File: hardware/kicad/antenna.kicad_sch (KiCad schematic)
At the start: 13 parts, among them J6 BWIPX-1-001E

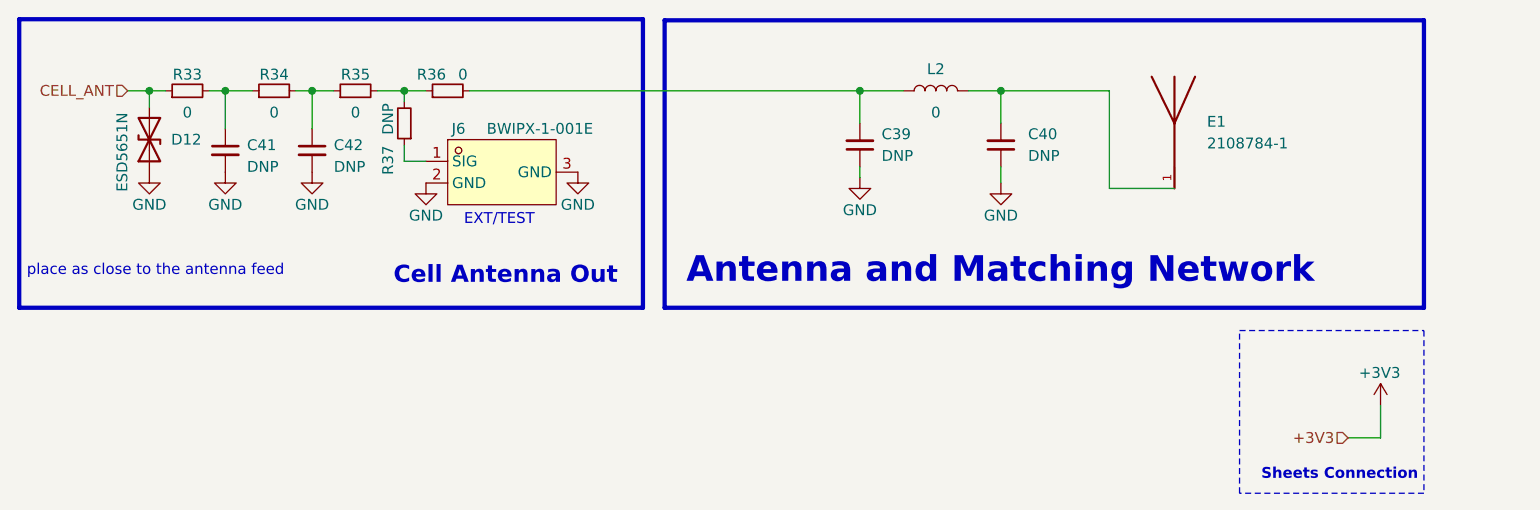
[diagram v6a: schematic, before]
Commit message: change antenna design
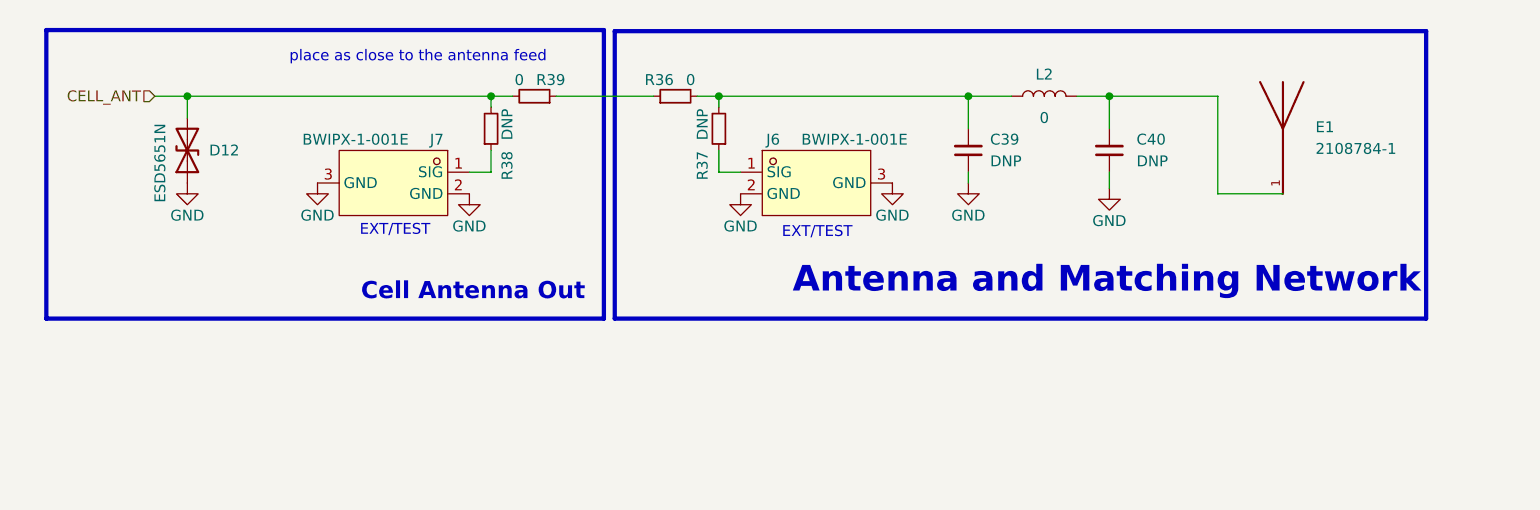
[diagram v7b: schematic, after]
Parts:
- removed C41, C42: DNP, Capacitor_SMD:C_0402_1005Metric, symbol Device:C_Small
- removed R33, R34, R35: 0, Resistor_SMD:R_0402_1005Metric, symbol Device:R_Small
- added J7: BWIPX-1-001E, bwlc1a:BWIPX-1-001E, symbol bwlc1a:BWIPX-1-001E
- added R38: DNP, Resistor_SMD:R_0402_1005Metric, symbol Device:R_Small
- added R39: 0, Resistor_SMD:R_0402_1005Metric, symbol Device:R_Small
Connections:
- net CELL_ANT: now also R38.2, R39.2
- net GND: now also J7.2 (GND), J7.3 (GND)
- net at R36.1: now also R39.1; no longer R37.2
- net at C39.2, L2.1, R36.2: now also R37.2
- new net: J7.1 (SIG), R38.1
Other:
- note removed: "Sheets Connection"
- moved on the sheet: C39, C40, D12, E1, J6, L2, R36, R37

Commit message: update
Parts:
- removed R37: DNP, Resistor_SMD:R_0402_1005Metric, symbol Device:R_Small
- added R33: DNP, Resistor_SMD:R_0402_1005Metric, symbol Device:R_Small
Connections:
- net at C39.2, L2.1, R36.2: now also R33.2
- net at J6.1 (SIG): now also R33.1
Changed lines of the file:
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@@
-	)
-	(symbol
-		(lib_id "Device:R_Small")
-		(at 153.67 93.98 180)
-		(unit 1)
-		(exclude_from_sim no)
-		(in_bom yes)
-		(on_board yes)
-		(dnp no)
-		(property "Reference" "R37"
-			(at 151.765 98.298 90)
-			(effects
-				(font
-					(size 1.27 1.27)
-				)
-			)
-		)
-		(property "Value" "DNP"
-			(at 151.765 93.472 90)
-			(effects
-				(font
-					(size 1.27 1.27)
-				)
-			)
-		)
-		(property "Footprint" "Resistor_SMD:R_0402_1005Metric"
-			(at 153.67 93.98 0)
-			(effects
-				(font
-					(size 1.27 1.27)
-				)
-				(hide yes)
-			)
-		)
-		(property "Datasheet" ""
-			(at 153.67 93.98 0)
-			(effects
-				(font
-					(size 1.27 1.27)
-				)
-				(hide yes)
-			)
-		)
-		(property "Description" ""
-			(at 153.67 93.98 0)
-			(effects
-				(font
-					(size 1.27 1.27)
-				)
-				(hide yes)
-			)
-		)
-		(property "Manufacturer" ""
-			(at 153.67 93.98 0)
-			(effects
-				(font
-					(size 1.27 1.27)
-				)
-				(hide yes)
-			)
-		)
-		(property "Manufacturer Part Number" ""
-			(at 153.67 93.98 0)
-			(effects
-				(font
-					(size 1.27 1.27)
-				)
-				(hide yes)
-			)
-		)
-		(property "Distributor" ""
-			(at 153.67 93.98 0)
-			(effects
-				(font
-					(size 1.27 1.27)
-				)
-				(hide yes)
-			)
-		)
-		(property "Distributor Part Number" ""
-			(at 153.67 93.98 0)
-			(effects
-				(font
-					(size 1.27 1.27)
-				)
-				(hide yes)
-			)
-		)
-		(property "Distributor Link" ""
-			(at 153.67 93.98 0)
-			(effects
-				(font
-					(size 1.27 1.27)
-				)
-				(hide yes)
-			)
-		)
-		(property "Id" ""
-			(at 153.67 93.98 0)
-			(effects
-				(font
-					(size 1.27 1.27)
-				)
-				(hide yes)
-			)
-		)
-		(property "Manufacture" ""
-			(at 153.67 93.98 0)
-			(effects
-				(font
-					(size 1.27 1.27)
-				)
-				(hide yes)
-			)
-		)
-		(property "Manufacture Part Number" ""
-			(at 153.67 93.98 0)
-			(effects
-				(font
-					(size 1.27 1.27)
-				)
-				(hide yes)
-			)
-		)
-		(property "Type" ""
-			(at 153.67 93.98 0)
-			(effects
-				(font
-					(size 1.27 1.27)
-				)
-				(hide yes)
-			)
-		)
-		(pin "1"
-		)
-		(pin "2"
-		)
-		(instances
-			(project "bwlc1a"
-				(path "/388039b1-99cc-430f-bd4a-010573fde798/ca79f09e-abdb-462a-9aab-98f2e37e5b23"
-					(reference "R37")
-					(unit 1)
-				)
-			)
-		)
 	)
 	(symbol
@@
 					(unit 1)
 				)
+			)
+		)
+	)
+	(symbol
+		(lib_id "Device:R_Small")
+		(at 153.67 93.98 0)
+		(mirror x)
+		(unit 1)
+		(exclude_from_sim no)
+		(in_bom yes)
+		(on_board yes)
+		(dnp no)
+		(property "Reference" "R33"
+			(at 150.876 98.298 90)
+			(effects
+				(font
+					(size 1.27 1.27)
+				)
+			)
+		)
+		(property "Value" "DNP"
+			(at 150.876 93.98 90)
+			(effects
+				(font
+					(size 1.27 1.27)
+				)
+			)
+		)
+		(property "Footprint" "Resistor_SMD:R_0402_1005Metric"
+			(at 153.67 93.98 0)
+			(effects
+				(font
+					(size 1.27 1.27)
+				)
+				(hide yes)
+			)
+		)
+		(property "Datasheet" ""
+			(at 153.67 93.98 0)
+			(effects
+				(font
+					(size 1.27 1.27)
+				)
+				(hide yes)
+			)
+		)
+		(property "Description" ""
+			(at 153.67 93.98 0)
+			(effects
+				(font
+					(size 1.27 1.27)
+				)
+				(hide yes)
+			)
+		)
+		(property "Manufacturer" ""
+			(at 153.67 93.98 0)
+			(effects
+				(font
+					(size 1.27 1.27)
+				)
+				(hide yes)
+			)
+		)
+		(property "Manufacturer Part Number" ""
+			(at 153.67 93.98 0)
+			(effects
+				(font
+					(size 1.27 1.27)
+				)
+				(hide yes)
+			)
+		)
+		(property "Distributor" ""
+			(at 153.67 93.98 0)
+			(effects
+				(font
+					(size 1.27 1.27)
+				)
+				(hide yes)
+			)
+		)
+		(property "Distributor Part Number" ""
+			(at 153.67 93.98 0)
+			(effects
+				(font
+					(size 1.27 1.27)
+				)
+				(hide yes)
+			)
+		)
+		(property "Distributor Link" ""
+			(at 153.67 93.98 0)
+			(effects
+				(font
+					(size 1.27 1.27)
+				)
+				(hide yes)
+			)
+		)
+		(property "Id" ""
+			(at 153.67 93.98 0)
+			(effects
+				(font
+					(size 1.27 1.27)
+				)
+				(hide yes)
+			)
+		)
+		(property "Manufacture" ""
+			(at 153.67 93.98 0)
+			(effects
+				(font
+					(size 1.27 1.27)
+				)
+				(hide yes)
+			)
+		)
+		(property "Manufacture Part Number" ""
+			(at 153.67 93.98 0)
+			(effects
+				(font
+					(size 1.27 1.27)
+				)
+				(hide yes)
+			)
+		)
+		(property "Type" ""
+			(at 153.67 93.98 0)
+			(effects
+				(font
+					(size 1.27 1.27)
+				)
+				(hide yes)
+			)
+		)
+		(pin "1"
+		)
+		(pin "2"
+		)
+		(instances
+			(project "bwlc1a"
+				(path "/388039b1-99cc-430f-bd4a-010573fde798/ca79f09e-abdb-462a-9aab-98f2e37e5b23"
+					(reference "R33")
+					(unit 1)
+				)
